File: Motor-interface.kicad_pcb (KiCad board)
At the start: 2 copper layers, 100.3 x 110.5 mm, 71 parts, among them J101 0, J102 0, J201 RJ45, J202 RJ45, P101 TE-23pins connector, P102 PSU_ISO, P103 Halls, P104 LineContactor, P105 ReverseContactor, P106 FanContactor, P107 Battery+, P108 MC_USB, P109 MC_CAN, P110 HallCurrent, Q101 Q_NPN_BCE, U101 AP1117D50, U102 AP1117D33, U103 TLP2361, U104 TLP2361, U105 TLP2361, U106 TLP2361, U107 TLP2361, U108 TLP2361, U109 Teensy_3.2, U110 TLP2361, U111 FODM3052, U201 TLP2361, U202 TLP2361, U203 MCP2551-I/SN, U301 MCP4251, U302 TLP2361, U303 TLP2361, U304 TLP2361, U305 TLP2361, U306 TLP290-4

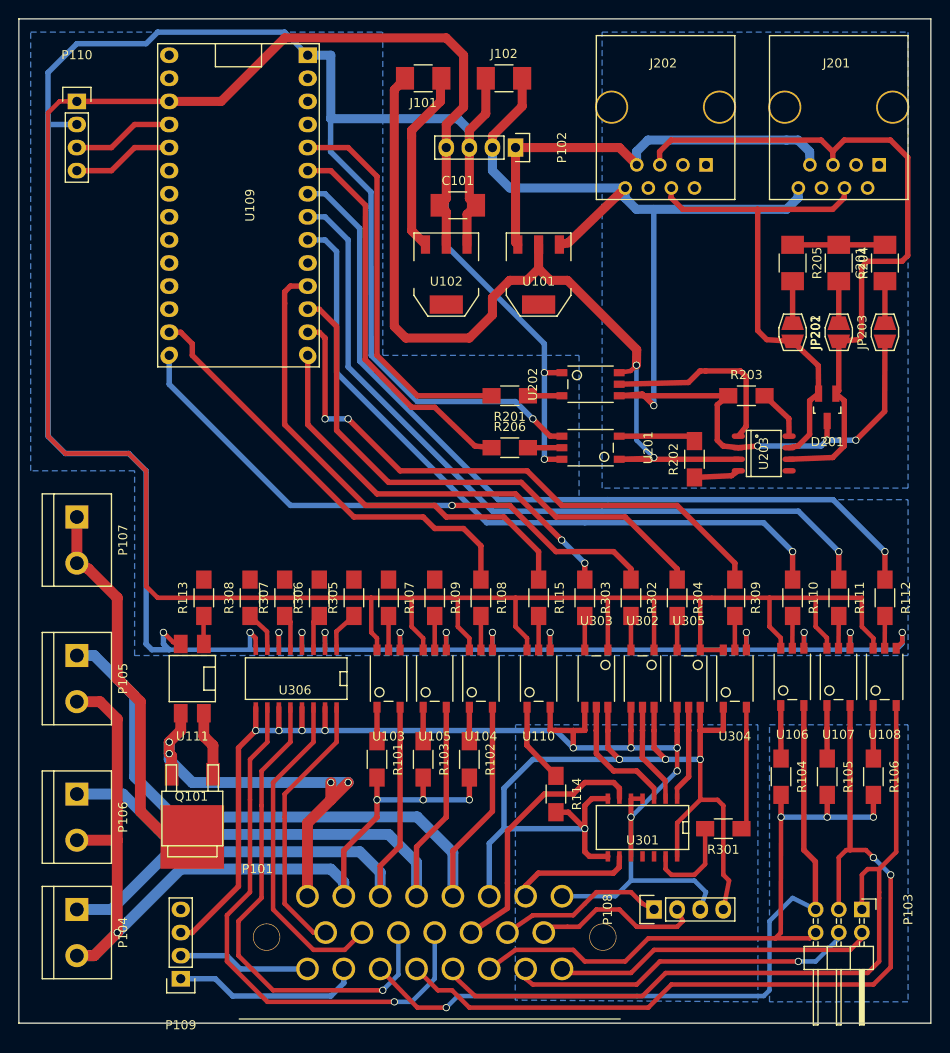
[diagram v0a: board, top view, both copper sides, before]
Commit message: laid out Contactors and monitors
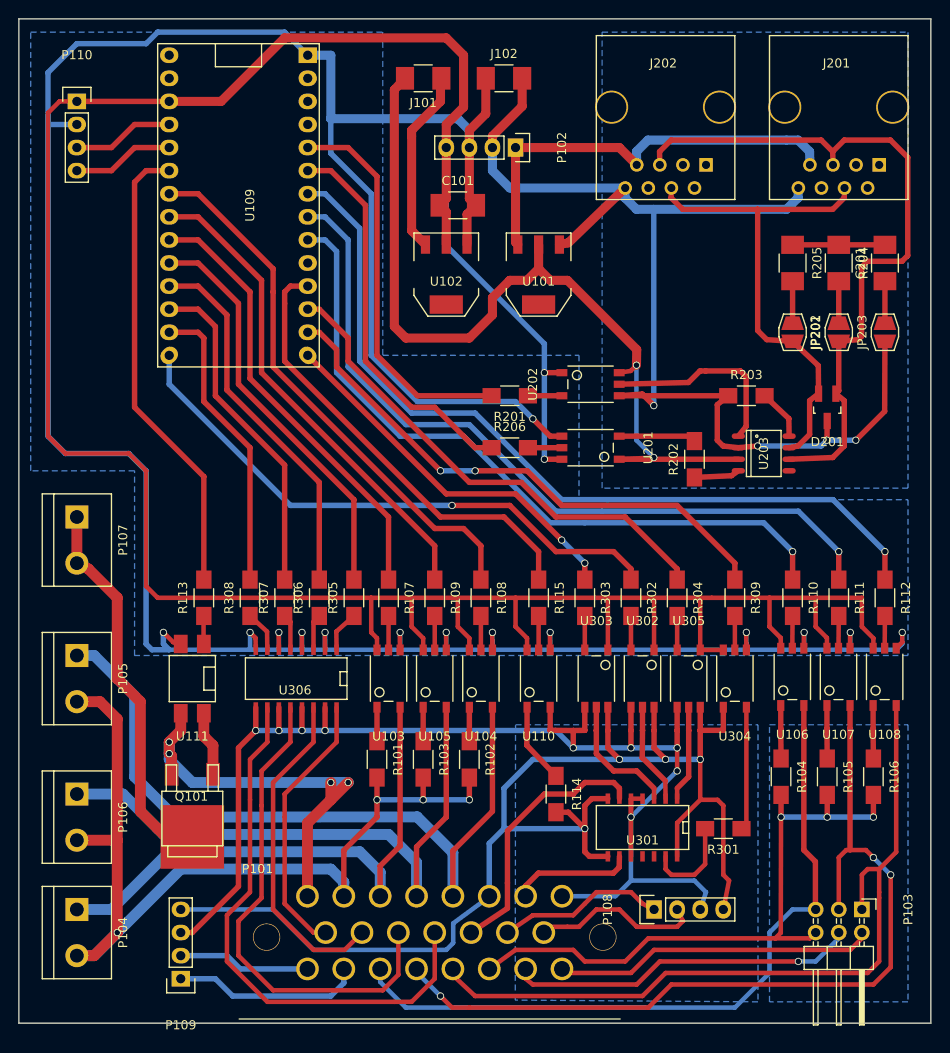
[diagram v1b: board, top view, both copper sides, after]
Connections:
- U109 pad 16: /Rev-Cont -> /PotsSwitches/Hybrid
- U109 pad 17: /Fan_Cont -> /PotsSwitches/Cruise
- U109 pad 18: /Line-Cont -> /PotsSwitches/Brake
- U109 pad 20: /PotsSwitches/Brake -> /Line-Cont
- U109 pad 21: /PotsSwitches/Cruise -> /Fan_Cont
- U109 pad 22: /PotsSwitches/Hybrid -> /Rev-Cont
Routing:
- net /Fan_Cont: track 0.00 -> 53.9 mm
- net /MOT_ON: track 0.00 -> 51.2 mm
- net /Line-Cont: track 0.00 -> 49.2 mm
- net /PotsSwitches/Reverse: track 0.00 -> 45.1 mm
- net /PotsSwitches/Brake: track 0.00 -> 41.0 mm
- net /PotsSwitches/Motor_5V: track 108.6 -> 148.0 mm
- net /PotsSwitches/Cruise: track 0.00 -> 36.9 mm
- net /PotsSwitches/Hybrid: track 0.00 -> 32.8 mm
- net /Rev-Cont: track 48.5 -> 60.4 mm
- net /PotsSwitches/DP-CS: track 60.3 -> 55.1 mm
- net /PotsSwitches/MOSI: track 46.2 -> 41.8 mm
- net /PotsSwitches/MISO: track 64.5 -> 60.4 mm
- net /Motor_Logic_On: track 54.2 -> 50.1 mm
- net /Motor-sensor-A: track 82.9 -> 81.0 mm, vias 1 -> 0
- net /Motor-sensor-B: track 95.0 -> 95.2 mm, vias 2 -> 3
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
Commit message: fixed triac, passed DRC
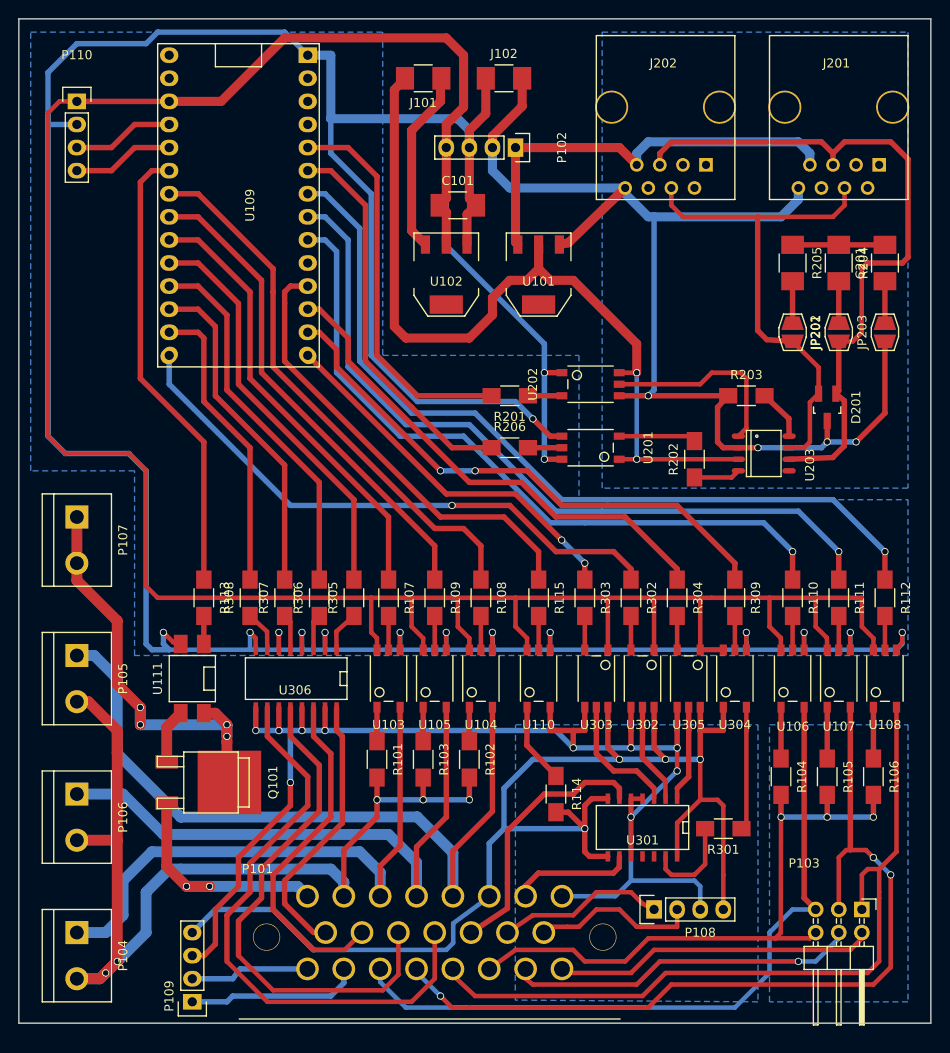
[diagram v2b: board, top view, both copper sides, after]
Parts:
- moved P109 2.84 mm to (62.3, 169.1)
- moved Q101 2.62 mm to (62.9, 145.0), turned to 270 degrees
- moved P104 2.54 mm to (49.6, 164.0)
- moved U106 0.19 mm to (128.3, 133.5)
- moved U107 0.19 mm to (133.4, 133.5)
- moved U108 0.19 mm to (138.5, 133.5)
- turned R113 to 270 degrees
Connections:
- Q101 pad 1: /on_triac -> Net-(Q101-Pad1)
- R113 pad 1: Net-(R113-Pad1) -> /MOT_ON
- R113 pad 2: /MOT_ON -> Net-(R113-Pad2)
- U111 pad 1: Net-(R113-Pad1) -> Net-(R113-Pad2)
- U111 pad 3: /On/Off-Switch -> Net-(Q101-Pad1)
- U111 pad 4: /on_triac -> /Battery+
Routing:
- net /On/Off-Switch: track 48.2 -> 27.0 mm, vias 4 -> 2
- net /Contactor+Common: track 103.7 -> 111.4 mm, vias 4 -> 5
- net /on_triac: track 7.13 -> 0.00 mm
- net /Battery+: track 42.4 -> 49.3 mm, vias 0 -> 4
- net Net-(Q101-Pad1): track 0.00 -> 5.98 mm
- net GNDA: track 132.4 -> 127.4 mm
- net +5VA: track 97.3 -> 93.1 mm
- net /PotsSwitches/Hybrid-Switch: track 60.6 -> 64.3 mm
- net /Line-contactor-coil: track 61.3 -> 64.6 mm
- net /PotsSwitches/Motor_GND: track 149.0 -> 152.2 mm, vias 9 -> 10
- net Net-(R113-Pad1): track 3.08 -> 0.00 mm
- net Net-(R113-Pad2): track 0.00 -> 3.08 mm
- net /PotsSwitches/Cruise-Switch: track 54.2 -> 56.8 mm
- net /Motor_CAN-L: track 20.9 -> 19.1 mm
- net /PotsSwitches/Brake-Switch: track 36.5 -> 38.1 mm
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
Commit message: renamed transistor
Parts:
- Q101: value Q_NPN_BCE -> NJD35N04G
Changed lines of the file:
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@@
       (effects (font (size 1 1) (thickness 0.15)))
     )
-    (fp_text value Q_NPN_BCE (at 5.715 -0.635 360) (layer F.Fab)
+    (fp_text value NJD35N04G (at 5.715 -0.635 360) (layer F.Fab)
       (effects (font (size 1 1) (thickness 0.15)))
     )
